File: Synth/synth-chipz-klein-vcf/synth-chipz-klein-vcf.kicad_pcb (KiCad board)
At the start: 2 copper layers, 45 x 22 mm, 57 parts, among them U1 TL074, U2 TL074

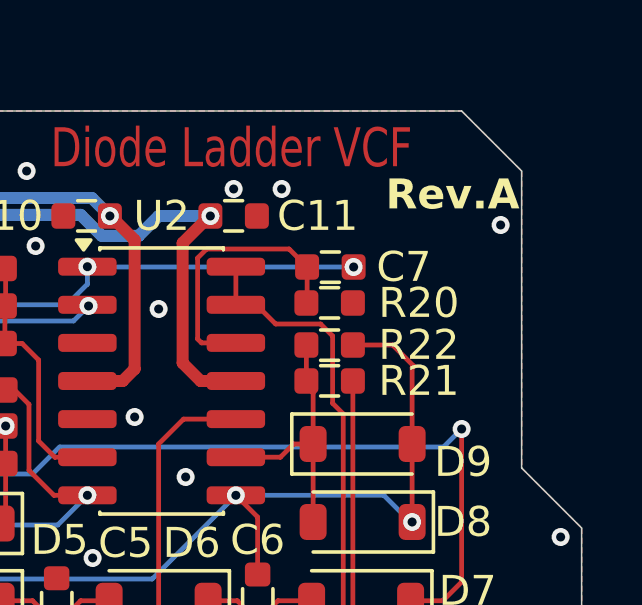
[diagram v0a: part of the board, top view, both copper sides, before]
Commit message: Correct swapped reference silk for R21,R22. Bump Rev.
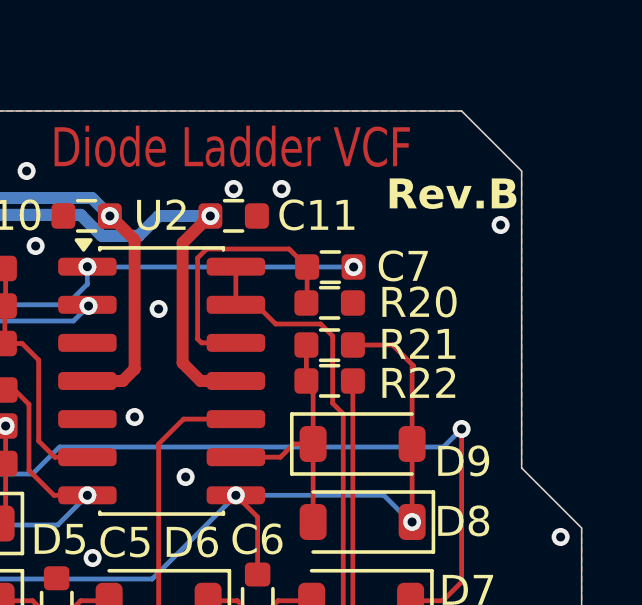
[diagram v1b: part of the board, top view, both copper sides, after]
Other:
- board text added: "PCB Design by: Circuit Monkey"
- board text added: "Rev. B (12/2025)"
- board text added: "Rev.B"
- board text removed: "PCB Design by: Circuit Monkey (11/2025)"
- board text removed: "Rev.A"
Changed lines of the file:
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@@
 	(title_block
 		(title "Synth CHIPz module - Klein VCF")
-		(date "2025-11-03")
-		(rev "A")
+		(date "2025-11-22")
+		(rev "B")
 		(company "Circuit Monkey")
 		(comment 1 "MIT License")
@@
 		(tags "capacitor")
 		(property "Reference" "R22"
-			(at 2.975 -1.2 0)
+			(at 2.975 0.1 0)
 			(layer "F.SilkS")
 			(effects
@@
 		(tags "capacitor")
 		(property "Reference" "R21"
-			(at -2.975 -1.2 0)
+			(at -2.975 0 0)
 			(layer "F.SilkS")
 			(effects
@@
 		)
 	)
-	(gr_text "Rev.A"
+	(gr_text "Rev.B"
 		(at 186.7 73.2 0)
 		(layer "F.SilkS")
@@
 		)
 	)
+	(gr_text "Rev. B  (12/2025)"
+		(at 167.8 88.1 0)
+		(layer "B.SilkS")
+		(effects
+			(font
+				(size 1 1)
+				(thickness 0.1)
+			)
+			(justify mirror)
+		)
+	)
 	(gr_text "Based on a circuit by: Moritz Klein"
 		(at 168.4 80.5 0)
@@
 		)
 	)
-	(gr_text "PCB Design by: Circuit Monkey (11/2025)"
+	(gr_text "PCB Design by: Circuit Monkey"
 		(at 167.7 89.7 0)
 		(layer "B.SilkS")
